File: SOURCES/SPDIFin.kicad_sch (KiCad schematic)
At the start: 20 parts, among them P18 TST, P31 CONN_01X03, U5 CS8422-CNZ

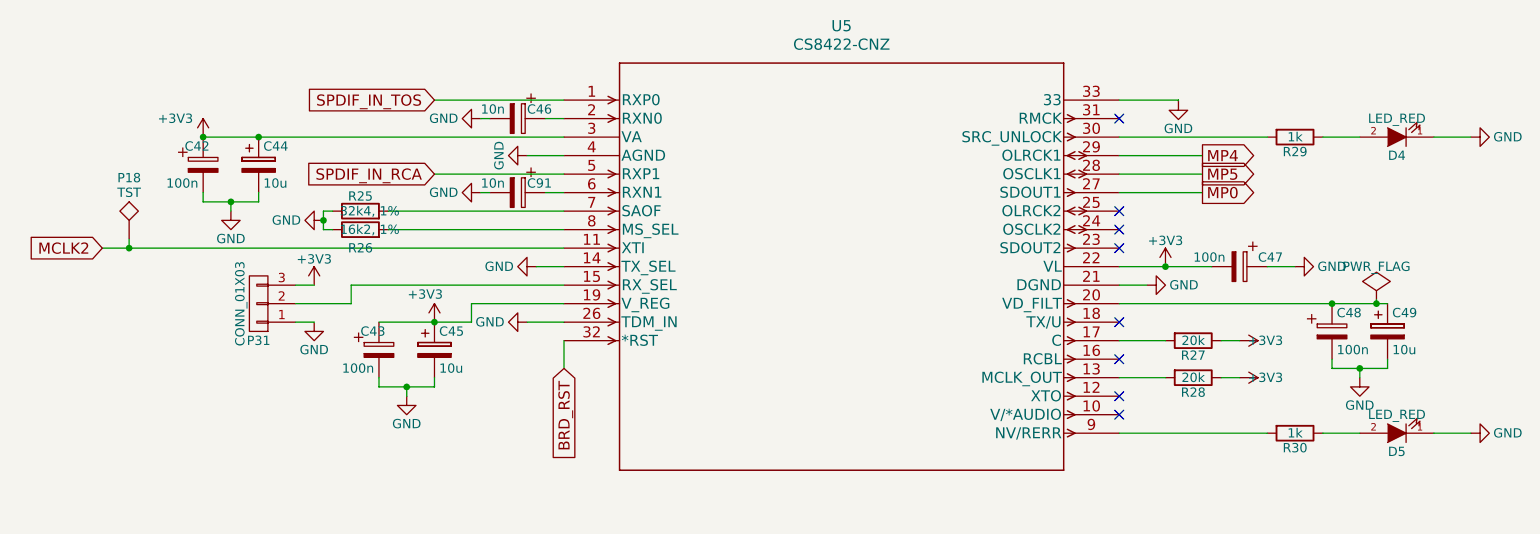
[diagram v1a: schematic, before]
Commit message: Removed ArduinoPort, Changed Power Supply. Rerouting and stuff.
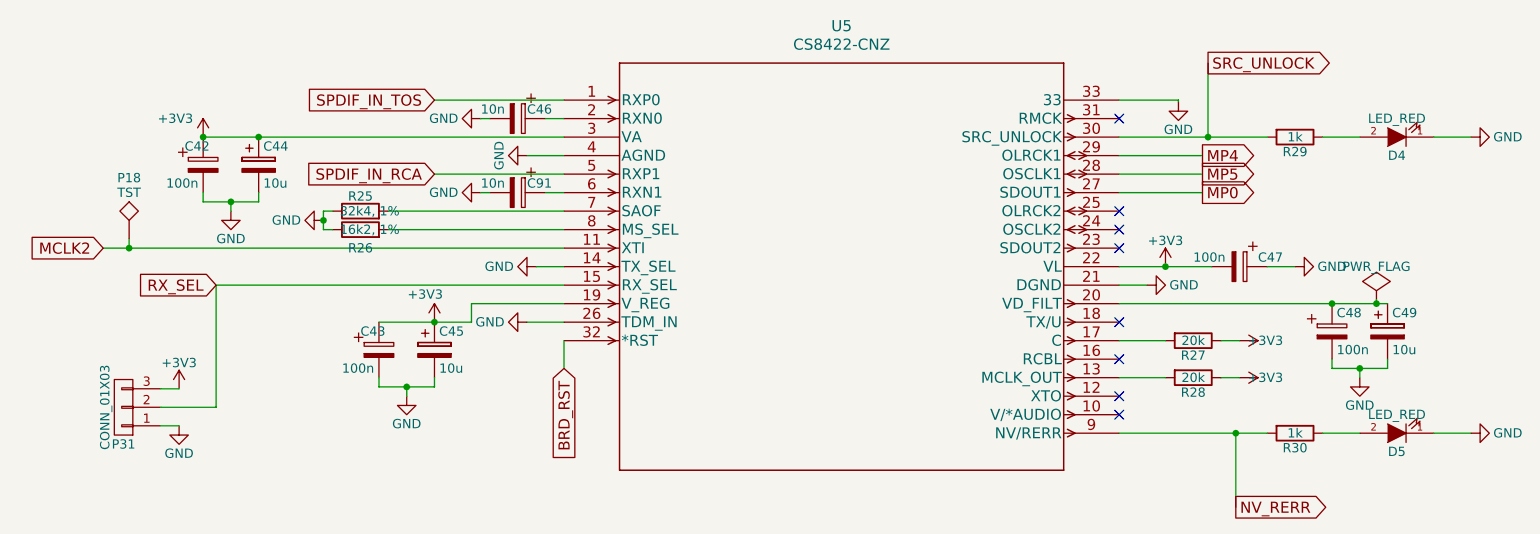
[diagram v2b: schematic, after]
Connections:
- net RX_SEL: now reaches P31.2 (P2), U5.15 (RX_SEL)
- net SRC_UNLOCK: now reaches R29.2, U5.30 (SRC_UNLOCK)
- net NV_RERR: now reaches R30.2, U5.9 (NV/RERR)
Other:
- moved on the sheet: P31
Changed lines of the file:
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@@
   (junction (at 87.63 119.38) (diameter 0) (color 0 0 0 0)
+  )
+  (junction (at 201.422 125.73) (diameter 0) (color 0 0 0 0)
+  )
+  (junction (at 197.612 85.09) (diameter 0) (color 0 0 0 0)
   )
   (junction (at 67.31 85.09) (diameter 0) (color 0 0 0 0)
@@
     (stroke (width 0) (type default))
   )
-  (wire (pts (xy 80.01 107.95) (xy 80.01 105.41))
+  (wire (pts (xy 61.468 122.174) (xy 61.468 105.41))
     (stroke (width 0) (type default))
   )
@@
     (stroke (width 0) (type default))
   )
+  (wire (pts (xy 201.422 135.89) (xy 201.422 125.73))
+    (stroke (width 0) (type default))
+  )
   (wire (pts (xy 83.82 119.38) (xy 87.63 119.38))
     (stroke (width 0) (type default))
@@
     (stroke (width 0) (type default))
   )
-  (wire (pts (xy 72.39 107.95) (xy 80.01 107.95))
+  (wire (pts (xy 53.848 122.174) (xy 61.468 122.174))
     (stroke (width 0) (type default))
   )
@@
     (stroke (width 0) (type default))
   )
-  (wire (pts (xy 45.847 100.33) (xy 49.53 100.33))
+  (wire (pts (xy 45.974 100.33) (xy 49.53 100.33))
     (stroke (width 0) (type default))
   )
@@
     (stroke (width 0) (type default))
   )
+  (wire (pts (xy 185.42 125.73) (xy 201.422 125.73))
+    (stroke (width 0) (type default))
+  )
   (wire (pts (xy 185.42 107.95) (xy 214.63 107.95))
     (stroke (width 0) (type default))
@@
     (stroke (width 0) (type default))
   )
+  (wire (pts (xy 197.612 85.09) (xy 205.74 85.09))
+    (stroke (width 0) (type default))
+  )
+  (wire (pts (xy 201.422 125.73) (xy 205.74 125.73))
+    (stroke (width 0) (type default))
+  )
   (wire (pts (xy 185.42 80.01) (xy 193.548 80.01))
     (stroke (width 0) (type default))
@@
     (stroke (width 0) (type default))
   )
-  (wire (pts (xy 185.42 125.73) (xy 205.74 125.73))
-    (stroke (width 0) (type default))
-  )
-  (wire (pts (xy 185.42 85.09) (xy 205.74 85.09))
+  (wire (pts (xy 185.42 85.09) (xy 197.612 85.09))
     (stroke (width 0) (type default))
   )
@@
     (stroke (width 0) (type default))
   )
-  (wire (pts (xy 80.01 105.41) (xy 109.22 105.41))
+  (wire (pts (xy 61.468 105.41) (xy 109.22 105.41))
     (stroke (width 0) (type default))
   )
@@
     (stroke (width 0) (type default))
   )
-  (wire (pts (xy 193.548 80.01) (xy 193.548 80.137))
-    (stroke (width 0) (type default))
-  )
-  (wire (pts (xy 72.39 110.49) (xy 74.93 110.49))
-    (stroke (width 0) (type default))
-  )
-  (wire (pts (xy 72.39 105.41) (xy 74.93 105.41))
+  (wire (pts (xy 193.548 80.01) (xy 193.548 80.264))
+    (stroke (width 0) (type default))
+  )
+  (wire (pts (xy 53.848 124.714) (xy 56.388 124.714))
+    (stroke (width 0) (type default))
+  )
+  (wire (pts (xy 53.848 119.634) (xy 56.388 119.634))
     (stroke (width 0) (type default))
   )
@@
   )
   (wire (pts (xy 228.6 85.09) (xy 233.68 85.09))
+    (stroke (width 0) (type default))
+  )
+  (wire (pts (xy 197.612 74.93) (xy 197.612 85.09))
     (stroke (width 0) (type default))
   )
@@
     )
   )
-  (global_label "MCLK2" (shape input) (at 45.847 100.33 180)
+  (global_label "RX_SEL" (shape input) (at 61.468 105.41 180) (fields_autoplaced)
     (effects (font (size 1.524 1.524)) (justify right))
-    (property "Intersheetrefs" "${INTERSHEET_REFS}" (at 45.847 100.33 0)
+    (property "Intersheetrefs" "${INTERSHEET_REFS}" (at 50.4707 105.41 0)
+      (effects (font (size 1.27 1.27)) (justify right) hide)
+    )
+  )
+  (global_label "SRC_UNLOCK" (shape output) (at 197.612 74.93 0) (fields_autoplaced)
+    (effects (font (size 1.524 1.524)) (justify left))
+    (property "Intersheetrefs" "${INTERSHEET_REFS}" (at 215.1408 74.93 0)
+      (effects (font (size 1.27 1.27)) (justify left) hide)
+    )
+  )
+  (global_label "NV_RERR" (shape output) (at 201.422 135.89 0) (fields_autoplaced)
+    (effects (font (size 1.524 1.524)) (justify left))
+    (property "Intersheetrefs" "${INTERSHEET_REFS}" (at 214.2337 135.89 0)
+      (effects (font (size 1.27 1.27)) (justify left) hide)
+    )
+  )
+  (global_label "MCLK2" (shape input) (at 45.974 100.33 180)
+    (effects (font (size 1.524 1.524)) (justify right))
+    (property "Intersheetrefs" "${INTERSHEET_REFS}" (at 45.974 100.33 0)
       (effects (font (size 1.27 1.27)) hide)
     )
@@
     )
   )
-  (symbol (lib_id "smd_aio-rescue:GND") (at 193.548 80.137 0) (unit 1)
-    (in_bom yes) (on_board yes) (dnp no)
-    (property "Reference" "#PWR085" (at 193.548 86.487 0)
-      (effects (font (size 1.27 1.27)) hide)
-    )
-    (property "Value" "GND" (at 193.548 83.947 0)
-      (effects (font (size 1.27 1.27)))
-    )
-    (property "Footprint" "" (at 193.548 80.137 0)
-      (effects (font (size 1.524 1.524)))
-    )
-    (property "Datasheet" "" (at 193.548 80.137 0)
+  (symbol (lib_id "smd_aio-rescue:GND") (at 193.548 80.264 0) (unit 1)
+    (in_bom yes) (on_board yes) (dnp no)
+    (property "Reference" "#PWR085" (at 193.548 86.614 0)
+      (effects (font (size 1.27 1.27)) hide)
+    )
+    (property "Value" "GND" (at 193.548 84.074 0)
+      (effects (font (size 1.27 1.27)))
+    )
+    (property "Footprint" "" (at 193.548 80.264 0)
+      (effects (font (size 1.524 1.524)))
+    )
+    (property "Datasheet" "" (at 193.548 80.264 0)
       (effects (font (size 1.524 1.524)))
     )
@@
     )
   )
-  (symbol (lib_id "smd_aio-rescue:GND") (at 74.93 110.49 0) (unit 1)
-    (in_bom yes) (on_board yes) (dnp no)
-    (property "Reference" "#PWR087" (at 74.93 116.84 0)
-      (effects (font (size 1.27 1.27)) hide)
-    )
-    (property "Value" "GND" (at 74.93 114.3 0)
-      (effects (font (size 1.27 1.27)))
-    )
-    (property "Footprint" "" (at 74.93 110.49 0)
-      (effects (font (size 1.524 1.524)))
-    )
-    (property "Datasheet" "" (at 74.93 110.49 0)
+  (symbol (lib_id "smd_aio-rescue:GND") (at 56.388 124.714 0) (unit 1)
+    (in_bom yes) (on_board yes) (dnp no)
+    (property "Reference" "#PWR087" (at 56.388 131.064 0)
+      (effects (font (size 1.27 1.27)) hide)
+    )
+    (property "Value" "GND" (at 56.388 128.524 0)
+      (effects (font (size 1.27 1.27)))
+    )
+    (property "Footprint" "" (at 56.388 124.714 0)
+      (effects (font (size 1.524 1.524)))
+    )
+    (property "Datasheet" "" (at 56.388 124.714 0)
       (effects (font (size 1.524 1.524)))
     )
@@
     )
   )
-  (symbol (lib_id "smd_aio-rescue:+3V3") (at 74.93 105.41 0) (unit 1)
-    (in_bom yes) (on_board yes) (dnp no)
-    (property "Reference" "#PWR088" (at 74.93 109.22 0)
-      (effects (font (size 1.27 1.27)) hide)
-    )
-    (property "Value" "+3V3" (at 74.93 101.854 0)
-      (effects (font (size 1.27 1.27)))
-    )
-    (property "Footprint" "" (at 74.93 105.41 0)
-      (effects (font (size 1.524 1.524)))
-    )
-    (property "Datasheet" "" (at 74.93 105.41 0)
+  (symbol (lib_id "smd_aio-rescue:+3V3") (at 56.388 119.634 0) (unit 1)
+    (in_bom yes) (on_board yes) (dnp no)
+    (property "Reference" "#PWR088" (at 56.388 123.444 0)
+      (effects (font (size 1.27 1.27)) hide)
+    )
+    (property "Value" "+3V3" (at 56.388 116.078 0)
+      (effects (font (size 1.27 1.27)))
+    )
+    (property "Footprint" "" (at 56.388 119.634 0)
+      (effects (font (size 1.524 1.524)))
+    )
+    (property "Datasheet" "" (at 56.388 119.634 0)
       (effects (font (size 1.524 1.524)))
     )
@@
     )
   )
-  (symbol (lib_id "smd_aio-rescue:CONN_01X03") (at 67.31 107.95 180) (unit 1)
-    (in_bom yes) (on_board yes) (dnp no)
-    (property "Reference" "P31" (at 67.31 113.03 0)
-      (effects (font (size 1.27 1.27)))
-    )
-    (property "Value" "CONN_01X03" (at 64.77 107.95 90)
-      (effects (font (size 1.27 1.27)))
-    )
-    (property "Footprint" "fdsp_pinheader:Pin_Header_Straight_1x03" (at 67.31 107.95 0)
+  (symbol (lib_id "smd_aio-rescue:CONN_01X03") (at 48.768 122.174 180) (unit 1)
+    (in_bom yes) (on_board yes) (dnp no)
+    (property "Reference" "P31" (at 48.768 127.254 0)
+      (effects (font (size 1.27 1.27)))
+    )
+    (property "Value" "CONN_01X03" (at 46.228 122.174 90)
+      (effects (font (size 1.27 1.27)))
+    )
+    (property "Footprint" "fdsp_pinheader:Pin_Header_Straight_1x03" (at 48.768 122.174 0)
       (effects (font (size 1.524 1.524)) hide)
     )
-    (property "Datasheet" "" (at 67.31 107.95 0)
-      (effects (font (size 1.524 1.524)))
-    )
+    (property "Datasheet" "" (at 48.768 122.174 0)
+      (effects (font (size 1.524 1.524)))
+    )
